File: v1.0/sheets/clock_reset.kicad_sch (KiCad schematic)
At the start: 13 parts, among them X1 32.768kHz, X2 16MHz

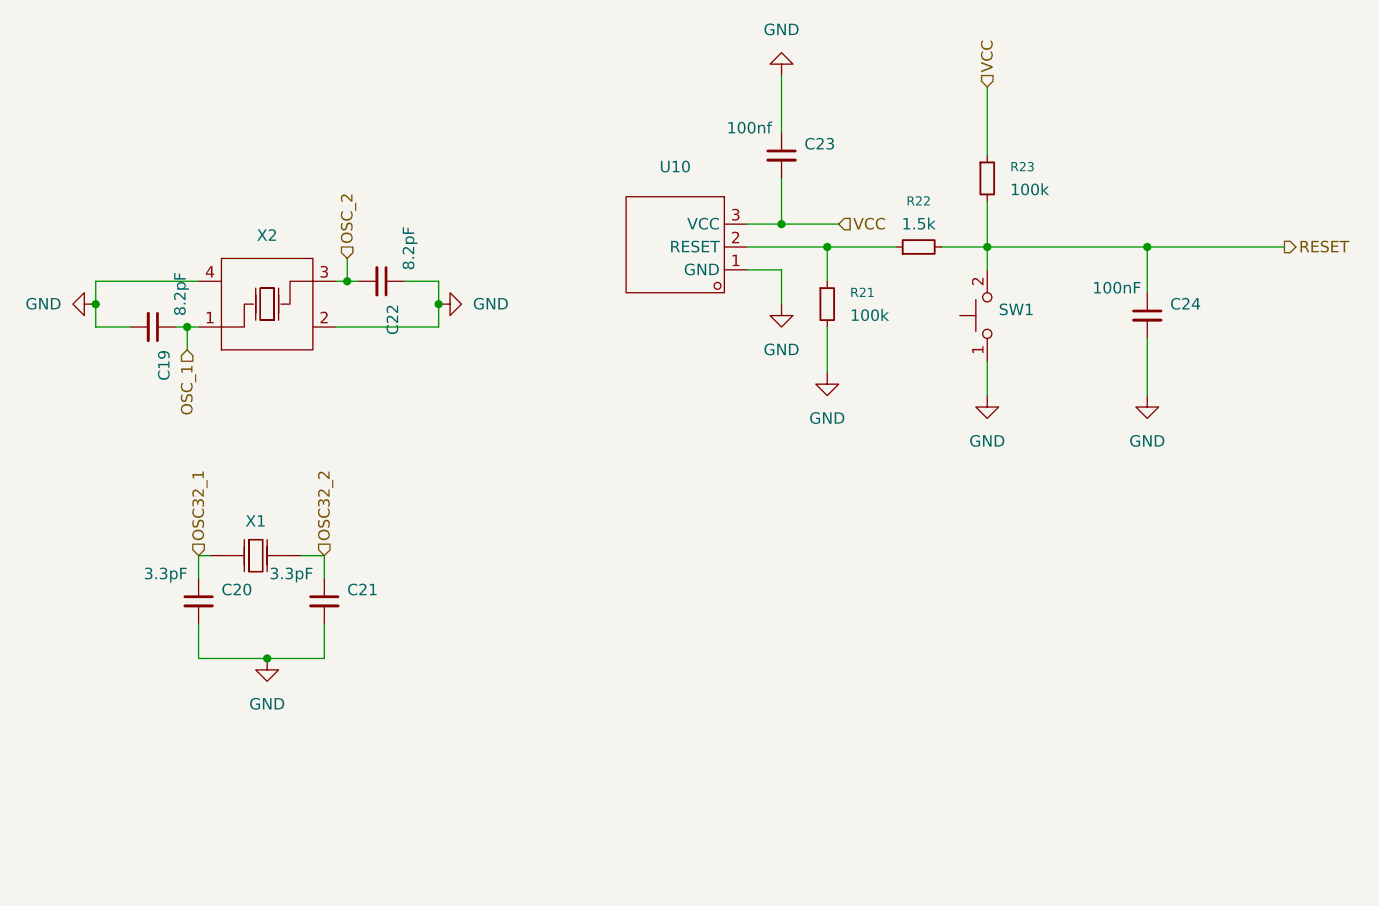
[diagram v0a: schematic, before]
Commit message: V1.0 rework to match stm32u5xxxQ
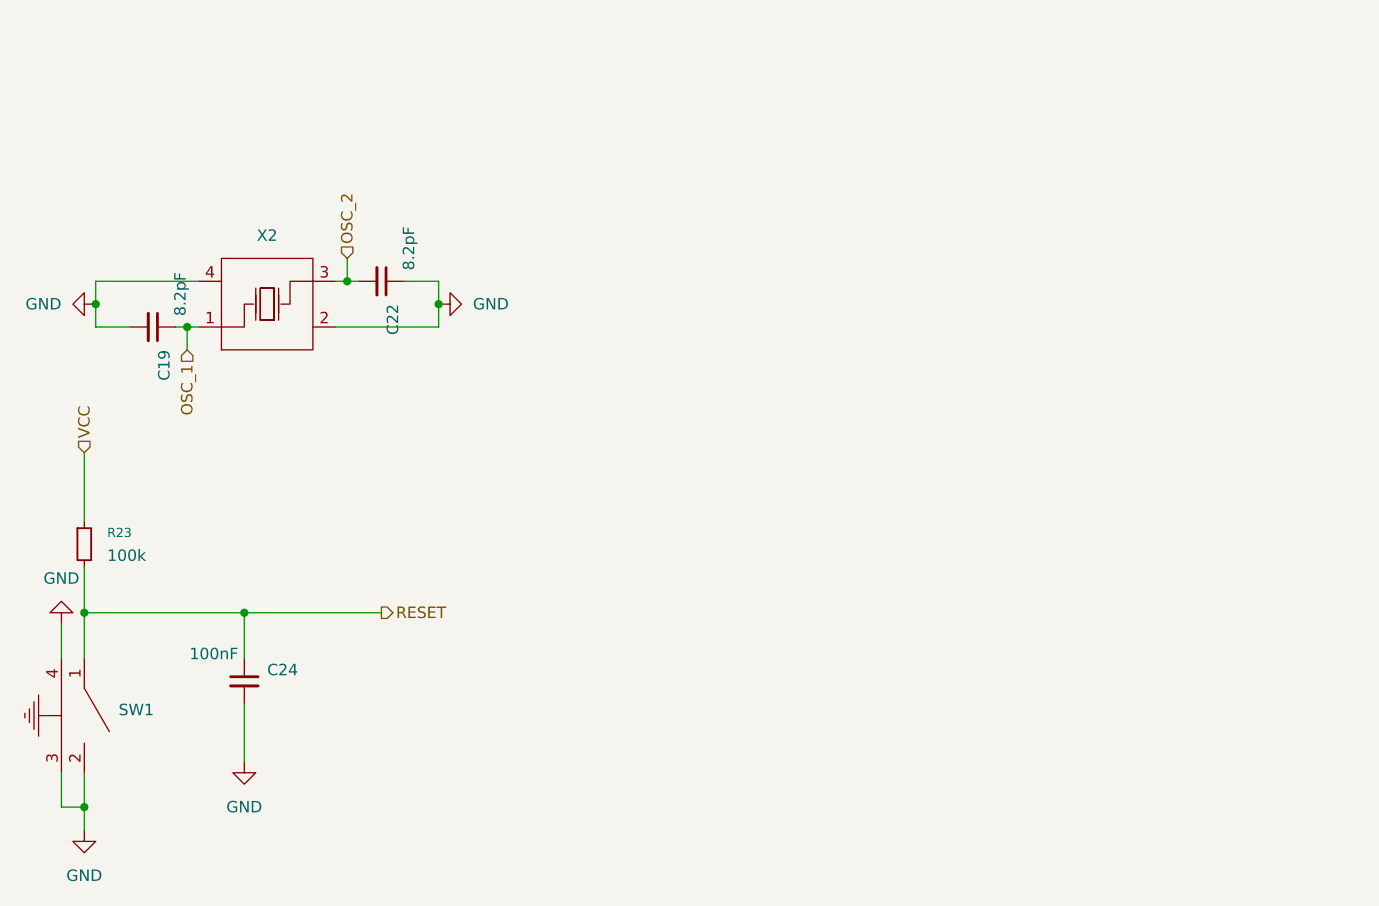
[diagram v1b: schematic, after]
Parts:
- removed C20, C21: 3.3pF, Capacitor_SMD:C_0402_1005Metric, symbol Device:C_Small
- removed C23: 100nf, Capacitor_SMD:C_0402_1005Metric, symbol Device:C_Small
- removed R21: 100k, Resistor_SMD:R_0402_1005Metric, symbol Device:R_Small
- removed R22: 1.5k, Resistor_SMD:R_0402_1005Metric, symbol Device:R_Small
- removed SW1: ~, Grinreflex:KEY-SMD_KSS-2G, symbol Grinreflex:KSS221GLFS
- removed U10: ~, Grinreflex:SOT-23-3_L2.9-W1.6-P1.90-LS2.8-BR, symbol Grinreflex:MAX809TEUR+T
- removed X1: 32.768kHz, Grinreflex:OSC-SMD_2P-L3.2-W1.5, symbol Grinreflex:ABS07-32.768KHZ-1-T
- added SW1: ~, Grinreflex:SW-SMD_YZA-021, symbol Grinreflex:YZA-021
- C24: footprint Capacitor_SMD:C_0603_1608Metric -> Capacitor_SMD:C_0402_1005Metric
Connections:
- net GND: now also SW1.2, SW1.3, SW1.4
- net RESET: now also SW1.1
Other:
- moved on the sheet: C24, R23
